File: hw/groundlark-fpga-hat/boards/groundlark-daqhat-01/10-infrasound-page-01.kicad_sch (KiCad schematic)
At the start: 2 parts, among them U23 DLVR-F50D

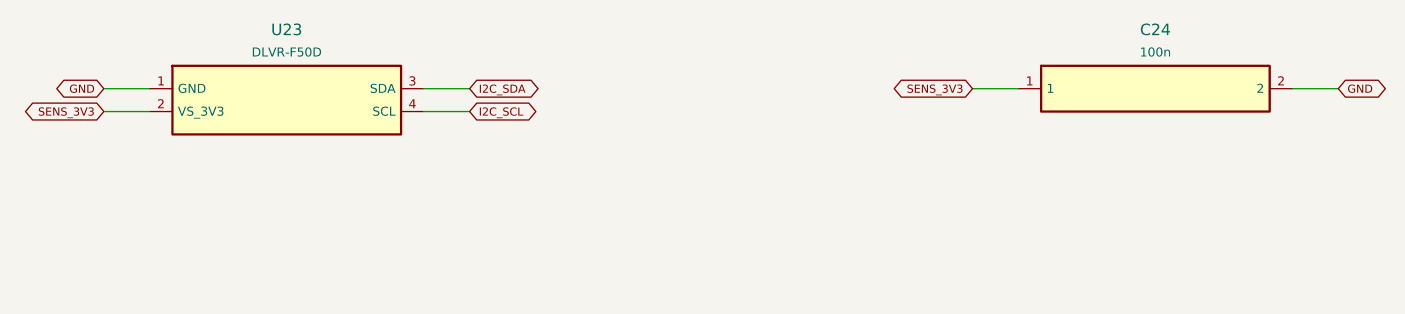
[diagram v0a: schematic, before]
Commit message: Update DAQHAT pressure sensor and assembly sourcing
Replace D90 with TPD2E2U06QDCKRQ1 and redesign U23 around SDP32-125PA. Synchronize routed CAD, native SES, models, supplier records, acquisition drivers, contracts, simulations, tests and documentation.

Record dated stock checks for 71 catalog identities and preserve the release gate for 52 unverified supplier placements. Generated manufacturing packages remain local and ignored.

Validation: repository structure and diff checks pass; prior full lab run passed 25 of 26 stages, with 301 software tests and 221 of 222 hardware tests passing. The remaining hardware test blocks unverified placements. Browser interaction and physical qualification remain pending.
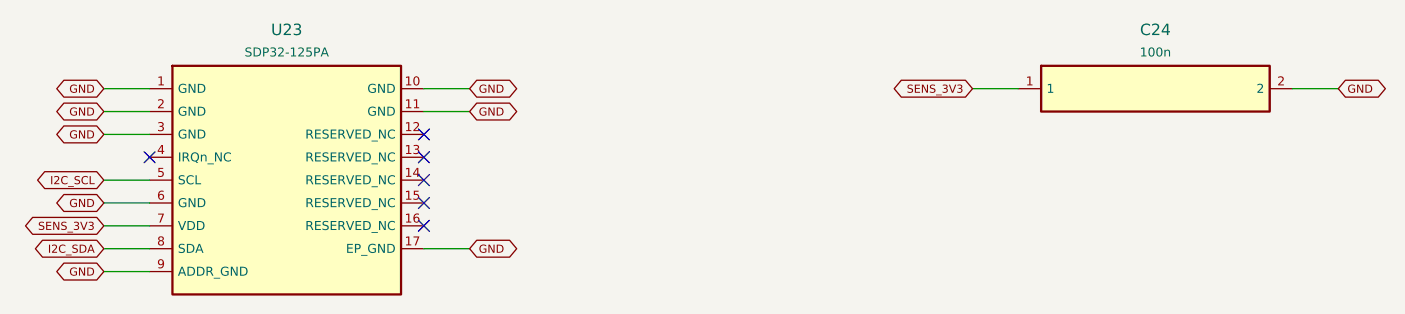
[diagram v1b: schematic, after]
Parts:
- U23: value DLVR-F50D -> SDP32-125PA; footprint Groundlark:Groundlark__DLVR_E1BS -> Groundlark:Groundlark__SDP32; MPN DLVR-F50D-E1BS-I-NI3F -> SDP32-125PA-TR-250PCS
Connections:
- net GND: now also U23.10 (GND), U23.11 (GND), U23.17 (EP_GND), U23.2 (GND), U23.3 (GND), U23.6 (GND), U23.9 (ADDR_GND)
- net I2C_SCL: now also U23.5 (SCL); no longer U23.4 (SCL)
- net I2C_SDA: now also U23.8 (SDA); no longer U23.3 (SDA)
- net SENS_3V3: now also U23.7 (VDD); no longer U23.2 (VS_3V3)
- no-connect marks 0 -> 6
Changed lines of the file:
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@@
 (kicad_sch (version 20230121) (generator eeschema) (paper "A3") (title_block (title "Groundlark DAQHAT-01 / 10-infrasound-page-01") (date "2026-09-30") (rev "DAQHAT-01"))
-(symbol (lib_id "Groundlark:Part_U23") (at 50.8 39.370000000000005 0) (unit 1) (in_bom yes) (on_board yes) (dnp no)
+(symbol (lib_id "Groundlark:Part_U23") (at 50.8 48.260000000000005 0) (unit 1) (in_bom yes) (on_board yes) (dnp no)
               (property "Reference" "U23" (at 50.8 31.560000000000002 0) (effects (font (size 1.27 1.27))))
-              (property "Value" "DLVR-F50D" (at 50.8 34.06 0) (effects (font (size 1.0 1.0))))
-              (property "Footprint" "Groundlark:Groundlark__DLVR_E1BS" (at 50.8 39.370000000000005 0) (effects (font (size 1 1)) hide))
-              (property "MPN" "DLVR-F50D-E1BS-I-NI3F" (at 50.8 39.370000000000005 0) (effects (font (size 1 1)) hide))
+              (property "Value" "SDP32-125PA" (at 50.8 34.06 0) (effects (font (size 1.0 1.0))))
+              (property "Footprint" "Groundlark:Groundlark__SDP32" (at 50.8 48.260000000000005 0) (effects (font (size 1 1)) hide))
+              (property "MPN" "SDP32-125PA-TR-250PCS" (at 50.8 48.260000000000005 0) (effects (font (size 1 1)) hide))
               (instances (project "groundlark-daqhat-01" (path "/de5c43d7-546f-5b4d-b587-d8dfceb38170/31d74753-b5b4-5f18-8597-e27d72686ce3" (reference "U23") (unit 1)))))
 (wire (pts (xy 35.56 38.1) (xy 30.48 38.1)) (stroke (width 0) (type default)))
 (global_label "GND" (shape bidirectional) (at 30.48 38.1 180) (effects (font (size 0.9 0.9)) (justify right)))
 (wire (pts (xy 35.56 40.64) (xy 30.48 40.64)) (stroke (width 0) (type default)))
-(global_label "SENS_3V3" (shape bidirectional) (at 30.48 40.64 180) (effects (font (size 0.9 0.9)) (justify right)))
+(global_label "GND" (shape bidirectional) (at 30.48 40.64 180) (effects (font (size 0.9 0.9)) (justify right)))
+(wire (pts (xy 35.56 43.18) (xy 30.48 43.18)) (stroke (width 0) (type default)))
+(global_label "GND" (shape bidirectional) (at 30.48 43.18 180) (effects (font (size 0.9 0.9)) (justify right)))
+(no_connect (at 35.56 45.72))
+(wire (pts (xy 35.56 48.26) (xy 30.48 48.26)) (stroke (width 0) (type default)))
+(global_label "I2C_SCL" (shape bidirectional) (at 30.48 48.26 180) (effects (font (size 0.9 0.9)) (justify right)))
+(wire (pts (xy 35.56 50.8) (xy 30.48 50.8)) (stroke (width 0) (type default)))
+(global_label "GND" (shape bidirectional) (at 30.48 50.8 180) (effects (font (size 0.9 0.9)) (justify right)))
+(wire (pts (xy 35.56 53.34) (xy 30.48 53.34)) (stroke (width 0) (type default)))
+(global_label "SENS_3V3" (shape bidirectional) (at 30.48 53.34 180) (effects (font (size 0.9 0.9)) (justify right)))
+(wire (pts (xy 35.56 55.88) (xy 30.48 55.88)) (stroke (width 0) (type default)))
+(global_label "I2C_SDA" (shape bidirectional) (at 30.48 55.88 180) (effects (font (size 0.9 0.9)) (justify right)))
+(wire (pts (xy 35.56 58.42) (xy 30.48 58.42)) (stroke (width 0) (type default)))
+(global_label "GND" (shape bidirectional) (at 30.48 58.42 180) (effects (font (size 0.9 0.9)) (justify right)))
 (wire (pts (xy 66.04 38.1) (xy 71.12 38.1)) (stroke (width 0) (type default)))
-(global_label "I2C_SDA" (shape bidirectional) (at 71.12 38.1 0) (effects (font (size 0.9 0.9)) (justify left)))
+(global_label "GND" (shape bidirectional) (at 71.12 38.1 0) (effects (font (size 0.9 0.9)) (justify left)))
 (wire (pts (xy 66.04 40.64) (xy 71.12 40.64)) (stroke (width 0) (type default)))
-(global_label "I2C_SCL" (shape bidirectional) (at 71.12 40.64 0) (effects (font (size 0.9 0.9)) (justify left)))
+(global_label "GND" (shape bidirectional) (at 71.12 40.64 0) (effects (font (size 0.9 0.9)) (justify left)))
+(no_connect (at 66.04 43.18))
+(no_connect (at 66.04 45.72))
+(no_connect (at 66.04 48.26))
+(no_connect (at 66.04 50.8))
+(no_connect (at 66.04 53.34))
+(wire (pts (xy 66.04 55.88) (xy 71.12 55.88)) (stroke (width 0) (type default)))
+(global_label "GND" (shape bidirectional) (at 71.12 55.88 0) (effects (font (size 0.9 0.9)) (justify left)))
 (symbol (lib_id "Groundlark:Part_C24") (at 147.32 38.1 0) (unit 1) (in_bom yes) (on_board yes) (dnp no)
               (property "Reference" "C24" (at 147.32 31.560000000000002 0) (effects (font (size 1.27 1.27))))
